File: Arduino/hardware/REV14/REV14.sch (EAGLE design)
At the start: 36 parts, among them IC1 LTC3525, IC2 ATMEGA168-AU, Q1 32768Hz, U1 RN2483, U2 TMP112, X1 SMA-142-0701-881/886, X2 SMA-142-0701-881/886

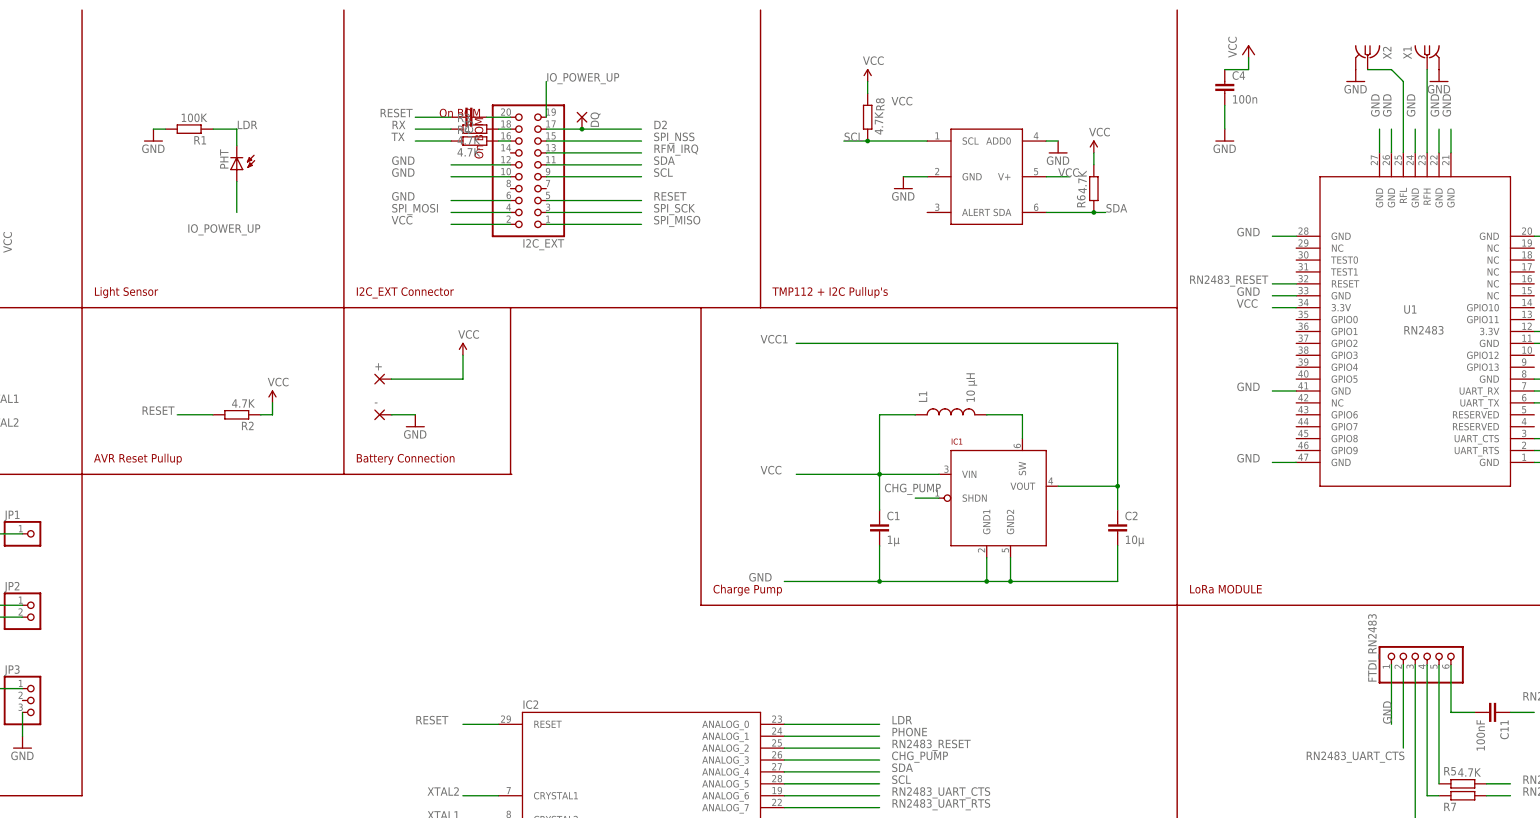
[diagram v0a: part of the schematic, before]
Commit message: added rough mobdect to rev14
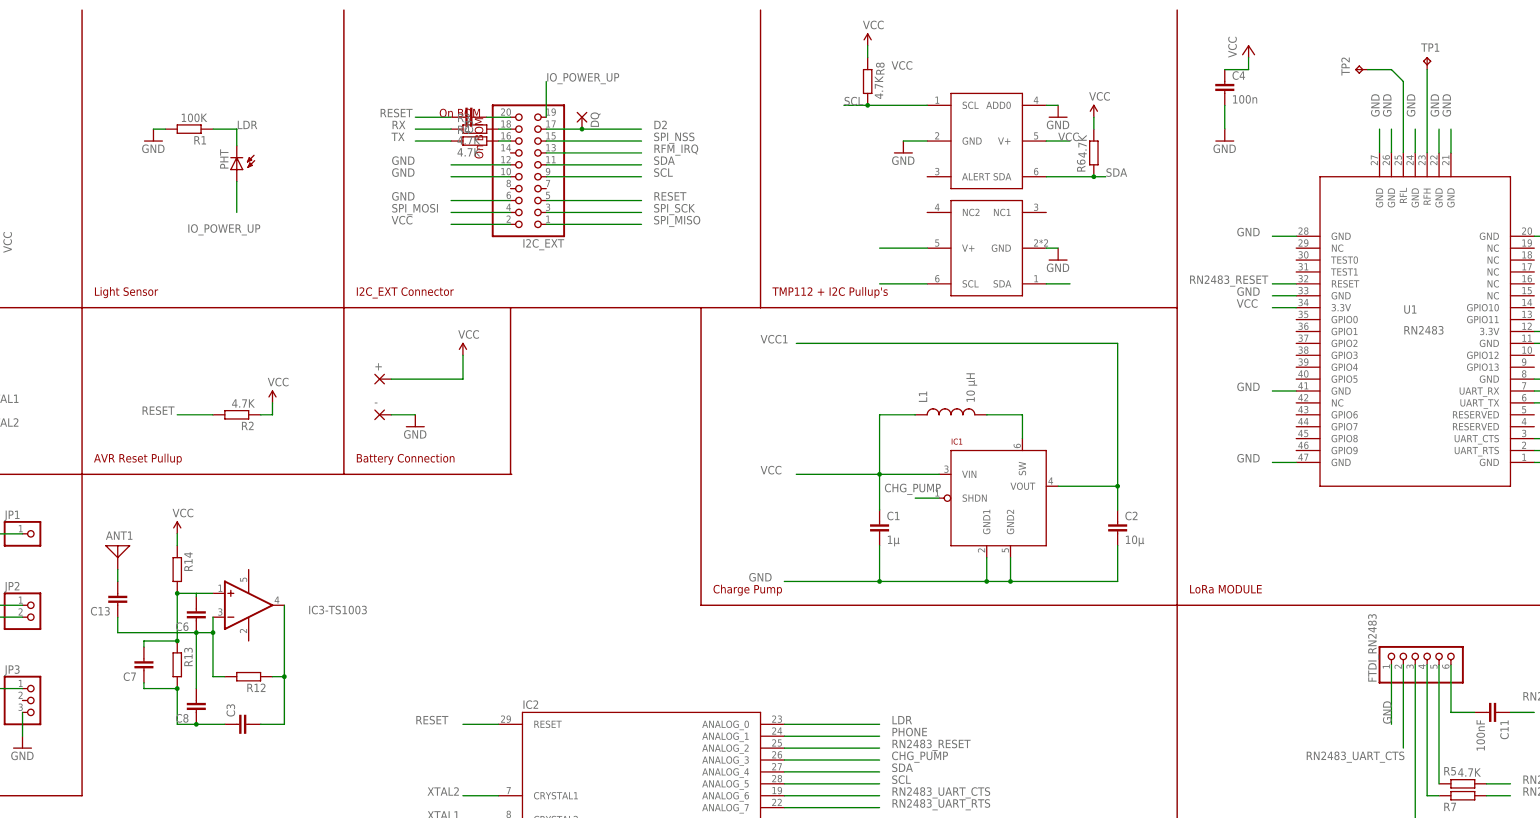
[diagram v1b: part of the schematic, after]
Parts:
- removed X1, X2: SMA-142-0701-881/886, con-coax:SMA-142-0701-881/886
- added ANT1: (no value), discrete:ANTENNA
- added C13, C3, C6, C7, C8: 1µ, SparkFun:CAP0603-CAP
- added IC3-TS1003: LM321MF, linear:LM321MF
- added R12, R13, R14: 4.7K, resistor:R-EU_R0603
- added TP1, TP2: TPB1,27, testpad:TPB1,27
- added U$4: SHT21, SHT21:SHT21
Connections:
- new net N$11: C13.1, C6.1, C8.2, IC3-TS1003.-IN, R12.2
- new net N$12: C3.2, IC3-TS1003.OUT, R12.1
- new net N$13: C3.1, C7.1, C8.1, R13.2
- new net N$14: C6.2, C7.2, IC3-TS1003.+IN, R13.1, R14.2
- new net N$15: ANT1.1, C13.2
- net GND: now also U$4.GND; no longer X1.2, X2.2
- net N$22: now also TP1.TP; no longer X1.1
- net N$33: now also TP2.TP; no longer X2.1
- net SCL: now also U$4.SCL
- net SDA: now also U$4.SDA
- net VCC: now also R14.1, U$4.V+
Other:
- moved on the sheet: R6, R8

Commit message: rev14 prerouting
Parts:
- removed ANT1: (no value), discrete:ANTENNA
- removed C13, C3, C6, C7, C8: 1µ, SparkFun:CAP0603-CAP
- removed IC3-TS1003: LM321MF, linear:LM321MF
- removed R12, R13, R14: 4.7K, resistor:R-EU_R0603
- added JP4: (no value), pinhead:PINHD-1X3
- C2: device SparkFun:CAP0805 -> rcl:C-EUC0603
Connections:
- removed net N$11: C13.1, C6.1, C8.2, IC3-TS1003.-IN, R12.2
- removed net N$12: C3.2, IC3-TS1003.OUT, R12.1
- removed net N$13: C3.1, C7.1, C8.1, R13.2
- removed net N$14: C6.2, C7.2, IC3-TS1003.+IN, R13.1, R14.2
- removed net N$15: ANT1.1, C13.2
- net CHG_PUMP: now also IC2.ANALOG_3
- net GND: now also JP4.3
- net RN2483_RESET: now also IC2.ANALOG_2
- net RN2483_UART_CTS: now also IC2.ANALOG_6
- net VCC: no longer R14.1
- net VCC1: now also JP4.1
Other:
- note added: "AVR Reset Pullup - on BOM - Locked"
- note added: "Battery Connection - on BOM - Locked"
- note added: "Crystal - on BOM - Locked"
- note added: "DS18B20 Pullup - on BOM - Locked"
- note added: "I2C_EXT Connector - on BOM - Locked"
- note added: "Light Sensor - on BOM - Locked"
- note added: "LoRa MODULE - on BOM - Locked"
- note added: "Mobile Detector MODULE - on BOM - Locked"
- note added: "Programming for LoRa MODULE - on BOM - Locked"
- note added: "TMP112 + SHT21 +I2C Pullup's - on BOM - Locked"
- note added: "VOICE MODULE - on BOM - Locked"
- note removed: "AVR Reset Pullup"
- note removed: "Battery Connection"
- note removed: "Crystal"
- note removed: "DS18B20 Pullup"
- note removed: "I2C_EXT Connector"
- note removed: "Light Sensor"
- note removed: "LoRa MODULE"
- note removed: "On BOM"
- note removed: "Programming for LoRa MODULE"
- note removed: "TMP112 + I2C Pullup's"
- note removed: "VOICE MODULE"
- moved on the sheet: C2

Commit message: rev 14 update
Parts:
- added R12, R13, R14, R15, R16, R17, R18: 4.7K, resistor:R-EU_R0603
- JP4: device pinhead:PINHD-1X3 -> pinhead:PINHD-1X4
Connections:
- new net N$11: IC2.ANALOG_6, R12.2
- new net N$12: IC2.ANALOG_7, R13.2
- new net N$13: IC2.ANALOG_2, R14.2
- new net N$14: FTDI_RN2483.2, R17.1
- new net N$16: JP4.2, R16.1
- new net N$17: I2C_EXT.12, R18.2
- net GND: now also R17.2, R18.1; no longer I2C_EXT.12
- net PHONE: now also R16.2
- net RN2483_RESET: now also R14.1, R15.2; no longer IC2.ANALOG_2
- net RN2483_UART_CTS: now also R12.1; no longer FTDI_RN2483.2, IC2.ANALOG_6
- net RN2483_UART_RTS: now also R13.1; no longer IC2.ANALOG_7
- net VCC: now also JP4.4, R15.1; no longer FTDI_RN2483.3
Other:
- note added: "Charge Pump - on BOM - Locked"
- note added: "Do NOT Pop"
- note removed: "Charge Pump"

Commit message: rev14 with mobile detect
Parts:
- added C13: 0.1uF, resistor:C-EUC0603
- added C3, C6: 22pF, resistor:C-EUC0603
- added C7: 0.22uF, resistor:C-EUC0603
- added C8: 100uF, resistor:C-EUC0603
- added IC3: TS1003IG5TMF, TS1003IG5T:TS1003IG5TMF
- added PAD1: (no value), wirepad:2,15/1,0
- added R19, R21: 2.2M, resistor:R-EU_R0603
- added R20: 100K, resistor:R-EU_R0603
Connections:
- new net N$18: C3.1, PAD1.P
- new net N$19: C3.2, C6.1, C7.2, IC3.-IN, R21.1
- new net N$21: C7.1, C8.1, IC3.+IN, R19.2, R20.1
- net GND: now also C13.2, C6.2, C8.2, IC3.V-, R20.2
- net PHONE: now also C13.1, IC3.OUT, R21.2
- net VCC: now also IC3.V+, R19.1
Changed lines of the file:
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@@
 <part name="R17" library="resistor" deviceset="R-EU_" device="R0603" value="4.7K"/>
 <part name="R18" library="resistor" deviceset="R-EU_" device="R0603" value="4.7K"/>
+<part name="IC3" library="TS1003IG5T" deviceset="TS1003IG5T" device="MF"/>
+<part name="C3" library="resistor" deviceset="C-EU" device="C0603" value="22pF"/>
+<part name="C6" library="resistor" deviceset="C-EU" device="C0603" value="22pF"/>
+<part name="C7" library="resistor" deviceset="C-EU" device="C0603" value="0.22uF"/>
+<part name="C8" library="resistor" deviceset="C-EU" device="C0603" value="100uF"/>
+<part name="R19" library="resistor" deviceset="R-EU_" device="R0603" value="2.2M"/>
+<part name="R20" library="resistor" deviceset="R-EU_" device="R0603" value="100K"/>
+<part name="R21" library="resistor" deviceset="R-EU_" device="R0603" value="2.2M"/>
+<part name="C13" library="resistor" deviceset="C-EU" device="C0603" value="0.1uF"/>
+<part name="PAD1" library="wirepad" deviceset="2,15/1,0" device=""/>
+<part name="GND5" library="SparkFun-Aesthetics" deviceset="GND" device=""/>
+<part name="P+6" library="SparkFun-Aesthetics" deviceset="VCC" device=""/>
+<part name="GND9" library="SparkFun-Aesthetics" deviceset="GND" device=""/>
 </parts>
 <sheets>
@@
 <text x="342.9" y="101.6" size="1.778" layer="95">Do NOT Pop</text>
 <text x="342.9" y="109.22" size="1.778" layer="95">Do NOT Pop</text>
+<wire x1="48.26" y1="88.9" x2="91.44" y2="88.9" width="0.3048" layer="94"/>
+<wire x1="91.44" y1="3.81" x2="91.44" y2="88.9" width="0.3048" layer="94"/>
 </plain>
 <instances>
@@
 </instance>
 <instance part="R18" gate="G$1" x="128.524" y="223.52"/>
+<instance part="IC3" gate="G$1" x="63.5" y="55.88"/>
+<instance part="C3" gate="G$1" x="12.7" y="55.88"/>
+<instance part="C6" gate="G$1" x="12.7" y="27.94"/>
+<instance part="C7" gate="G$1" x="27.94" y="55.88"/>
+<instance part="C8" gate="G$1" x="25.4" y="27.94"/>
+<instance part="R19" gate="G$1" x="40.64" y="63.5" smashed="yes" rot="R270">
+<attribute name="NAME" x="37.0586" y="62.23" size="1.778" layer="95" rot="R270"/>
+<attribute name="VALUE" x="37.338" y="67.31" size="1.778" layer="96" rot="R270"/>
+</instance>
+<instance part="R20" gate="G$1" x="40.64" y="27.94" smashed="yes" rot="R270">
+<attribute name="NAME" x="37.0586" y="26.67" size="1.778" layer="95" rot="R270"/>
+<attribute name="VALUE" x="37.338" y="31.75" size="1.778" layer="96" rot="R270"/>
+</instance>
+<instance part="R21" gate="G$1" x="60.96" y="38.1" smashed="yes">
+<attribute name="NAME" x="62.23" y="34.5186" size="1.778" layer="95"/>
+<attribute name="VALUE" x="57.15" y="34.798" size="1.778" layer="96"/>
+</instance>
+<instance part="C13" gate="G$1" x="76.2" y="30.48"/>
+<instance part="PAD1" gate="1" x="12.7" y="68.58" rot="R270"/>
+<instance part="GND5" gate="1" x="40.64" y="15.24"/>
+<instance part="P+6" gate="G$1" x="40.64" y="71.12"/>
+<instance part="GND9" gate="1" x="63.5" y="43.18"/>
 </instances>
 <busses>
@@
 <pinref part="GND4" gate="1" pin="GND"/>
 <wire x1="76.2" y1="137.16" x2="83.82" y2="137.16" width="0.1524" layer="91"/>
+</segment>
+<segment>
+<pinref part="C6" gate="G$1" pin="2"/>
+<pinref part="C8" gate="G$1" pin="2"/>
+<wire x1="12.7" y1="22.86" x2="25.4" y2="22.86" width="0.1524" layer="91"/>
+<pinref part="R20" gate="G$1" pin="2"/>
+<wire x1="25.4" y1="22.86" x2="40.64" y2="22.86" width="0.1524" layer="91"/>
+<junction x="25.4" y="22.86"/>
+<pinref part="GND5" gate="1" pin="GND"/>
+<wire x1="40.64" y1="17.78" x2="40.64" y2="22.86" width="0.1524" layer="91"/>
+<junction x="40.64" y="22.86"/>
+<pinref part="C13" gate="G$1" pin="2"/>
+<wire x1="40.64" y1="22.86" x2="76.2" y2="22.86" width="0.1524" layer="91"/>
+<wire x1="76.2" y1="22.86" x2="76.2" y2="25.4" width="0.1524" layer="91"/>
+</segment>
+<segment>
+<pinref part="GND9" gate="1" pin="GND"/>
+<wire x1="63.5" y1="45.72" x2="63.5" y2="48.26" width="0.1524" layer="91"/>
+<pinref part="IC3" gate="G$1" pin="V-"/>
 </segment>
 </net>
@@
 <pinref part="R15" gate="G$1" pin="1"/>
 </segment>
+<segment>
+<pinref part="R19" gate="G$1" pin="1"/>
+<pinref part="P+6" gate="G$1" pin="VCC"/>
+<wire x1="40.64" y1="68.58" x2="40.64" y2="71.12" width="0.1524" layer="91"/>
+<pinref part="IC3" gate="G$1" pin="V+"/>
+<wire x1="63.5" y1="63.5" x2="63.5" y2="68.58" width="0.1524" layer="91"/>
+<wire x1="63.5" y1="68.58" x2="40.64" y2="68.58" width="0.1524" layer="91"/>
+<junction x="40.64" y="68.58"/>
+</segment>
 </net>
 <net name="SPI_SCK" class="0">
@@
 <junction x="58.42" y="129.54"/>
 </segment>
+<segment>
+<pinref part="IC3" gate="G$1" pin="OUT"/>
+<wire x1="71.12" y1="55.88" x2="76.2" y2="55.88" width="0.1524" layer="91"/>
+<wire x1="76.2" y1="55.88" x2="76.2" y2="38.1" width="0.1524" layer="91"/>
+<pinref part="R21" gate="G$1" pin="2"/>
+<wire x1="76.2" y1="38.1" x2="66.04" y2="38.1" width="0.1524" layer="91"/>
+<pinref part="C13" gate="G$1" pin="1"/>
+<wire x1="76.2" y1="33.02" x2="76.2" y2="38.1" width="0.1524" layer="91"/>
+<junction x="76.2" y="38.1"/>
+<label x="78.74" y="58.42" size="1.778" layer="95"/>
+</segment>
 </net>
 <net name="N$11" class="0">
@@
 </segment>
 </net>
+<net name="N$18" class="0">
+<segment>
+<pinref part="PAD1" gate="1" pin="P"/>
+<pinref part="C3" gate="G$1" pin="1"/>
+<wire x1="12.7" y1="66.04" x2="12.7" y2="58.42" width="0.1524" layer="91"/>
+</segment>
+</net>
+<net name="N$19" class="0">
+<segment>
+<pinref part="C3" gate="G$1" pin="2"/>
+<pinref part="C6" gate="G$1" pin="1"/>
+<wire x1="12.7" y1="50.8" x2="12.7" y2="30.48" width="0.1524" layer="91"/>
+<pinref part="C7" gate="G$1" pin="2"/>
+<wire x1="12.7" y1="50.8" x2="27.94" y2="50.8" width="0.1524" layer="91"/>
+<junction x="12.7" y="50.8"/>
+<pinref part="IC3" gate="G$1" pin="-IN"/>
+<wire x1="27.94" y1="50.8" x2="48.26" y2="50.8" width="0.1524" layer="91"/>
+<wire x1="48.26" y1="50.8" x2="55.88" y2="50.8" width="0.1524" layer="91"/>
+<wire x1="55.88" y1="50.8" x2="55.88" y2="53.34" width="0.1524" layer="91"/>
+<junction x="27.94" y="50.8"/>
+<pinref part="R21" gate="G$1" pin="1"/>
+<wire x1="55.88" y1="38.1" x2="48.26" y2="38.1" width="0.1524" layer="91"/>
+<wire x1="48.26" y1="38.1" x2="48.26" y2="50.8" width="0.1524" layer="91"/>
+<junction x="48.26" y="50.8"/>
+</segment>
+</net>
+<net name="N$21" class="0">
+<segment>
+<pinref part="C8" gate="G$1" pin="1"/>
+<wire x1="25.4" y1="30.48" x2="25.4" y2="33.02" width="0.1524" layer="91"/>
+<pinref part="R20" gate="G$1" pin="1"/>
+<wire x1="25.4" y1="33.02" x2="40.64" y2="33.02" width="0.1524" layer="91"/>
+<pinref part="C7" gate="G$1" pin="1"/>
+<pinref part="R19" gate="G$1" pin="2"/>
+<wire x1="27.94" y1="58.42" x2="40.64" y2="58.42" width="0.1524" layer="91"/>
+<wire x1="40.64" y1="33.02" x2="40.64" y2="58.42" width="0.1524" layer="91"/>
+<junction x="40.64" y="33.02"/>
+<junction x="40.64" y="58.42"/>
+<pinref part="IC3" gate="G$1" pin="+IN"/>
+<wire x1="40.64" y1="58.42" x2="55.88" y2="58.42" width="0.1524" layer="91"/>
+</segment>
+</net>

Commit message: rev14 routed
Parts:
- C7: device resistor:C-EUC0603 -> rcl:C-EU050H075X075
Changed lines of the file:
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@@
 <part name="C3" library="resistor" deviceset="C-EU" device="C0603" value="22pF"/>
 <part name="C6" library="resistor" deviceset="C-EU" device="C0603" value="22pF"/>
-<part name="C7" library="resistor" deviceset="C-EU" device="C0603" value="0.22uF"/>
+<part name="C7" library="rcl" deviceset="C-EU" device="050H075X075" value="0.22uF"/>
 <part name="C8" library="resistor" deviceset="C-EU" device="C0603" value="100uF"/>
 <part name="R19" library="resistor" deviceset="R-EU_" device="R0603" value="2.2M"/>

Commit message: rev 14 ready for gerbers
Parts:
- removed TP2: TPB1,27, testpad:TPB1,27
- added PAD2, PAD3: (no value), wirepad:3,81/1,4
- added TP4: TPSQTP06R, testpad:TPSQTP06R
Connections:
- net N$22: now also PAD3.P
- net N$33: now also PAD2.P, TP4.TP; no longer TP2.TP
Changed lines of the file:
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@@
 <part name="GND8" library="SparkFun-Aesthetics" deviceset="GND" device=""/>
 <part name="TP1" library="testpad" deviceset="TP" device="B1,27"/>
-<part name="TP2" library="testpad" deviceset="TP" device="B1,27"/>
 <part name="GND12" library="SparkFun-Aesthetics" deviceset="GND" device=""/>
 <part name="U$4" library="SHT21" deviceset="SHT21" device=""/>
@@
 <part name="P+6" library="SparkFun-Aesthetics" deviceset="VCC" device=""/>
 <part name="GND9" library="SparkFun-Aesthetics" deviceset="GND" device=""/>
+<part name="PAD2" library="wirepad" deviceset="3,81/1,4" device=""/>
+<part name="PAD3" library="wirepad" deviceset="3,81/1,4" device=""/>
+<part name="TP4" library="testpad" deviceset="TPSQ" device="TP06R"/>
 </parts>
 <sheets>
@@
 <instance part="GND8" gate="1" x="35.56" y="99.06"/>
 <instance part="TP1" gate="G$1" x="335.28" y="246.38"/>
-<instance part="TP2" gate="G$1" x="320.04" y="243.84" rot="R90"/>
 <instance part="GND12" gate="1" x="256.54" y="203.2"/>
 <instance part="U$4" gate="G$1" x="241.3" y="205.74"/>
@@
 <instance part="P+6" gate="G$1" x="40.64" y="71.12"/>
 <instance part="GND9" gate="1" x="63.5" y="43.18"/>
+<instance part="PAD2" gate="1" x="327.66" y="246.38" rot="R270"/>
+<instance part="PAD3" gate="1" x="337.82" y="241.3" rot="R180"/>
+<instance part="TP4" gate="G$1" x="317.5" y="241.3"/>
 </instances>
 <busses>
@@
 <wire x1="228.6" y1="205.74" x2="218.44" y2="205.74" width="0.1524" layer="91"/>
 <pinref part="U$4" gate="G$1" pin="V+"/>
+<label x="213.36" y="205.74" size="1.778" layer="95"/>
 </segment>
 <segment>
@@
 <wire x1="254" y1="198.12" x2="259.08" y2="198.12" width="0.1524" layer="91"/>
 <pinref part="U$4" gate="G$1" pin="SDA"/>
+<label x="256.54" y="195.58" size="1.778" layer="95"/>
 </segment>
 </net>
@@
 <wire x1="218.44" y1="198.12" x2="228.6" y2="198.12" width="0.1524" layer="91"/>
 <pinref part="U$4" gate="G$1" pin="SCL"/>
+<label x="213.36" y="198.12" size="1.778" layer="95"/>
 </segment>
 </net>
@@
 <segment>
 <pinref part="U1" gate="G$1" pin="RFH"/>
-<wire x1="335.28" y1="226.06" x2="335.28" y2="243.84" width="0.1524" layer="91"/>
+<wire x1="335.28" y1="226.06" x2="335.28" y2="241.3" width="0.1524" layer="91"/>
 <pinref part="TP1" gate="G$1" pin="TP"/>
+<pinref part="PAD3" gate="1" pin="P"/>
+<wire x1="335.28" y1="241.3" x2="335.28" y2="243.84" width="0.1524" layer="91"/>
+<junction x="335.28" y="241.3"/>
 </segment>
 </net>
@@
 <wire x1="330.2" y1="226.06" x2="330.2" y2="241.3" width="0.1524" layer="91"/>
 <wire x1="330.2" y1="241.3" x2="327.66" y2="243.84" width="0.1524" layer="91"/>
-<wire x1="327.66" y1="243.84" x2="322.58" y2="243.84" width="0.1524" layer="91"/>
-<pinref part="TP2" gate="G$1" pin="TP"/>
-</segment>
-</net>
+<wire x1="327.66" y1="243.84" x2="317.5" y2="243.84" width="0.1524" layer="91"/>
+<pinref part="PAD2" gate="1" pin="P"/>
+<junction x="327.66" y="243.84"/>
+<pinref part="TP4" gate="G$1" pin="TP"/>
+</segment>
+</net>
